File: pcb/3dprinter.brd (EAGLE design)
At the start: 100 x 80 mm, 111 parts, among them IC1 NRF51822, IC1_REG REGULATOR, IC2_REG LP2985-3V3, Q1_BED MOSFET, Q1_FAN1 MOSFETSOT23, Q1_FAN2 MOSFETSOT23, Q1_NOZ MOSFET, Y1 CRYSTAL

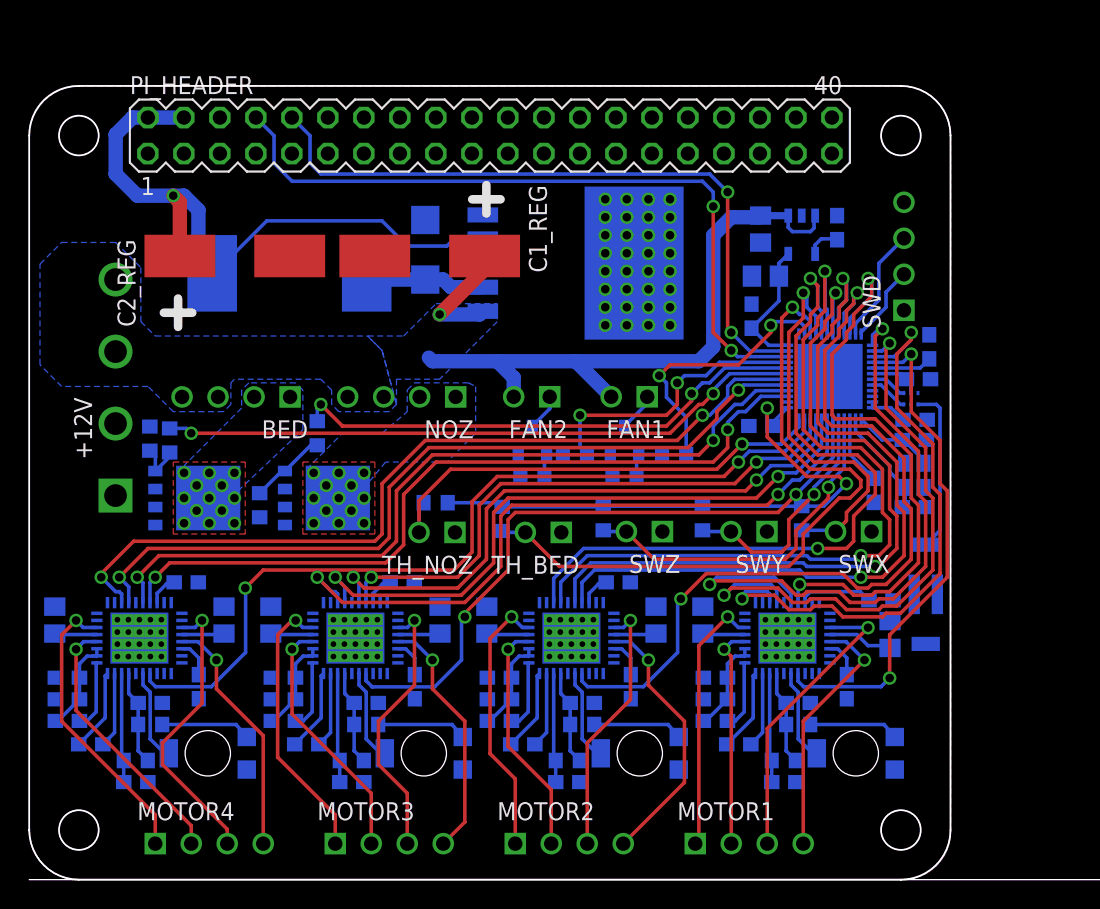
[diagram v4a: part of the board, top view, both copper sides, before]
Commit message: Component placement done, started final routing
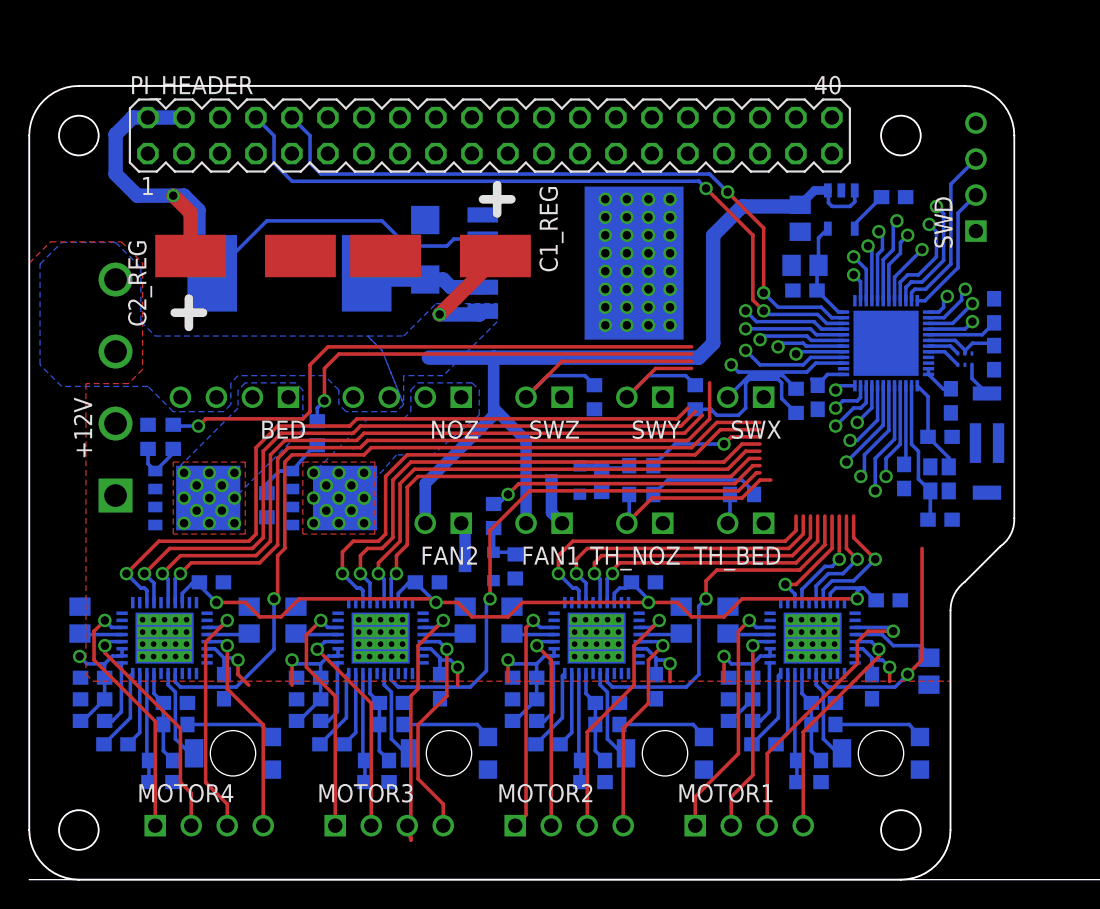
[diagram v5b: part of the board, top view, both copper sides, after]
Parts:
- moved R3_BED 17.0 mm to (50.3, 27.2), turned to 180 degrees
- moved TH_NOZ 14.7 mm to (42.2, 25.1)
- moved R3_NOZ 14.5 mm to (43.2, 27.2)
- moved TH_BED 14.3 mm to (49.3, 25.1)
- moved SWX 12.2 mm to (49.3, 34.0)
- moved SWY 12.0 mm to (42.2, 34.0)
- moved SWZ 11.8 mm to (35.1, 34.0)
- moved ANT 11.5 mm to (67.6, 30.8)
- moved FAN2 10.9 mm to (27.9, 25.1)
- moved FAN1 10.8 mm to (35.1, 25.1)
- moved Q1_FAN2 9.66 mm to (31.8, 22.1), turned to 180 degrees
- moved R1_SWZ 8.56 mm to (39.9, 34.0), turned to 270 degrees
- moved R1_SWY 8.55 mm to (47.0, 34.0), turned to 270 degrees
- moved R1_SWX 8.29 mm to (54.1, 33.8), turned to 270 degrees
- moved SWD 7.55 mm to (66.8, 49.6)
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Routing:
- net +12V: track 91.0 -> 134.9 mm, vias 1 -> 9
- net THBED: track 49.1 -> 5.56 mm
- net STEP_M1: track 44.3 -> 10.3 mm
- net +3V3: track 62.4 -> 95.1 mm, vias 2 -> 4
- net DIR_M2: track 54.3 -> 24.0 mm
- net CFG2_M1: track 41.6 -> 11.9 mm
- net CFG1_M1: track 40.9 -> 11.2 mm
- net CFG1_M2: track 54.5 -> 27.4 mm
- net STEP_M2: track 51.4 -> 25.6 mm
- net EN_M2: track 57.8 -> 32.9 mm
- net CFG2_M2: track 52.2 -> 27.7 mm
- net DIR_M1: track 41.1 -> 17.6 mm
- net THNOZ: track 34.0 -> 15.0 mm
- net SWX: track 27.9 -> 9.81 mm
- net EN_M1: track 36.0 -> 19.7 mm
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- added copper zone on layer 1, net +12V
- removed copper zone on layer 1, net GND
- removed copper zone on layer 16, net GND

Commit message: More routing
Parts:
- added SJ1, SJ2, SJ3, SJ4, SJ5, SJ6, SJ7, SJ8: (no value), 3dprinter:SJ_2
- moved R1_FAN2 11.6 mm to (43.2, 30.7), turned to 0 degrees
- moved Q1_FAN2 6.18 mm to (30.7, 28.2)
- moved R2_FAN2 6.18 mm to (33.3, 28.2)
- moved R2_M1 1.62 mm to (62.3, 13.6)
- moved C14 0.25 mm to (55.6, 33.8)
- moved C6_M4 0.25 mm to (13.1, 21.0)
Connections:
- new net P0.08: IC1.14
- new net P0.09: IC1.15
- new net P0.10: IC1.16
- new net P0.11: IC1.17
- new net P0.12: IC1.18
- new net P0.13: IC1.19
- new net P0.17: IC1.25
- new net P0.21: IC1.40
- net +3V3: now also SJ1.3, SJ2.3, SJ3.3, SJ4.3, SJ5.3, SJ6.3, SJ7.3, SJ8.3
- net BED: now also IC1.9; no longer IC1.7
- net CFG1_M1: now also SJ1.2; no longer IC1.26
- net CFG1_M2: now also SJ3.2; no longer IC1.18
- net CFG1_M3: now also SJ5.2; no longer IC1.44
- net CFG1_M4: now also SJ7.2; no longer IC1.5
- net CFG2_M1: now also SJ2.2; no longer IC1.27
- net CFG2_M2: now also SJ4.2; no longer IC1.17
- net CFG2_M3: now also SJ6.2; no longer IC1.43
- net CFG2_M4: now also SJ8.2; no longer IC1.6
- net DIR_M1: now also IC1.27; no longer IC1.22
- net DIR_M2: now also IC1.21; no longer IC1.20
- net DIR_M3: now also IC1.42; no longer IC1.46
- net DIR_M4: now also IC1.46; no longer IC1.3
- net EN_M2: now also IC1.22; no longer IC1.21
- net EN_M3: now also IC1.41; no longer IC1.42
- net EN_M4: now also IC1.45; no longer IC1.47
- net FAN1: now also IC1.43; no longer IC1.14
- net FAN2: now also IC1.48; no longer IC1.9
- net GND: now also SJ1.1, SJ2.1, SJ3.1, SJ4.1, SJ5.1, SJ6.1, SJ7.1, SJ8.1
- net STEP_M1: now also IC1.26; no longer IC1.25
- net STEP_M2: now also IC1.20; no longer IC1.19
- net STEP_M3: now also IC1.44; no longer IC1.45
- net STEP_M4: now also IC1.47; no longer IC1.4
- net SWX: now also IC1.3; no longer IC1.16
- net SWY: now also IC1.4; no longer IC1.41
- net SWZ: now also IC1.5; no longer IC1.40
- net THBED: now also IC1.6; no longer IC1.15
- net THNOZ: now also IC1.7; no longer IC1.48
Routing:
- net +3V3: track 95.1 -> 170.5 mm, vias 4 -> 13
- net CFG2_M4: track 55.6 -> 5.44 mm, vias 2 -> 1
- net CFG1_M4: track 52.9 -> 10.5 mm, vias 2 -> 1
- net CFG2_M3: track 46.2 -> 7.08 mm, vias 2 -> 1
- net CFG1_M3: track 42.4 -> 12.9 mm, vias 2 -> 1
- net STEP_M1: track 10.3 -> 33.8 mm
- net DIR_M2: track 24.0 -> 46.9 mm
- net STEP_M2: track 25.6 -> 46.9 mm
- net CFG2_M2: track 27.7 -> 7.37 mm, vias 2 -> 1
- net EN_M2: track 32.9 -> 52.1 mm
- net EN_M1: track 19.7 -> 38.5 mm
- net EN_M3: track 45.8 -> 64.2 mm
- net THBED: track 5.56 -> 23.8 mm
- net THNOZ: track 15.0 -> 32.5 mm
- net CFG1_M2: track 27.4 -> 12.7 mm, vias 2 -> 1
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- added copper zone on layer 1, net GND
- added copper zone on layer 16, net GND

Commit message: Final routing first pass
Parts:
- moved C1 0.80 mm to (67.3, 36.6)
- moved BAL 0.51 mm to (65.5, 36.7)
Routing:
- net GND: track 0.00 -> 68.0 mm, vias 32 -> 44
- net +3V3: track 170.5 -> 179.0 mm, vias 13 -> 15
- net OB1_M3: track 19.1 -> 17.2 mm
- net IC1_VDD_PA: track 5.62 -> 4.61 mm
- net ANT: track 2.76 -> 3.43 mm
- net IC1_ANT2: track 2.28 -> 1.77 mm
- net IC1_ANT1: track 2.44 -> 1.94 mm
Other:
- board size 100 x 80 mm -> 69.5 x 56 mm

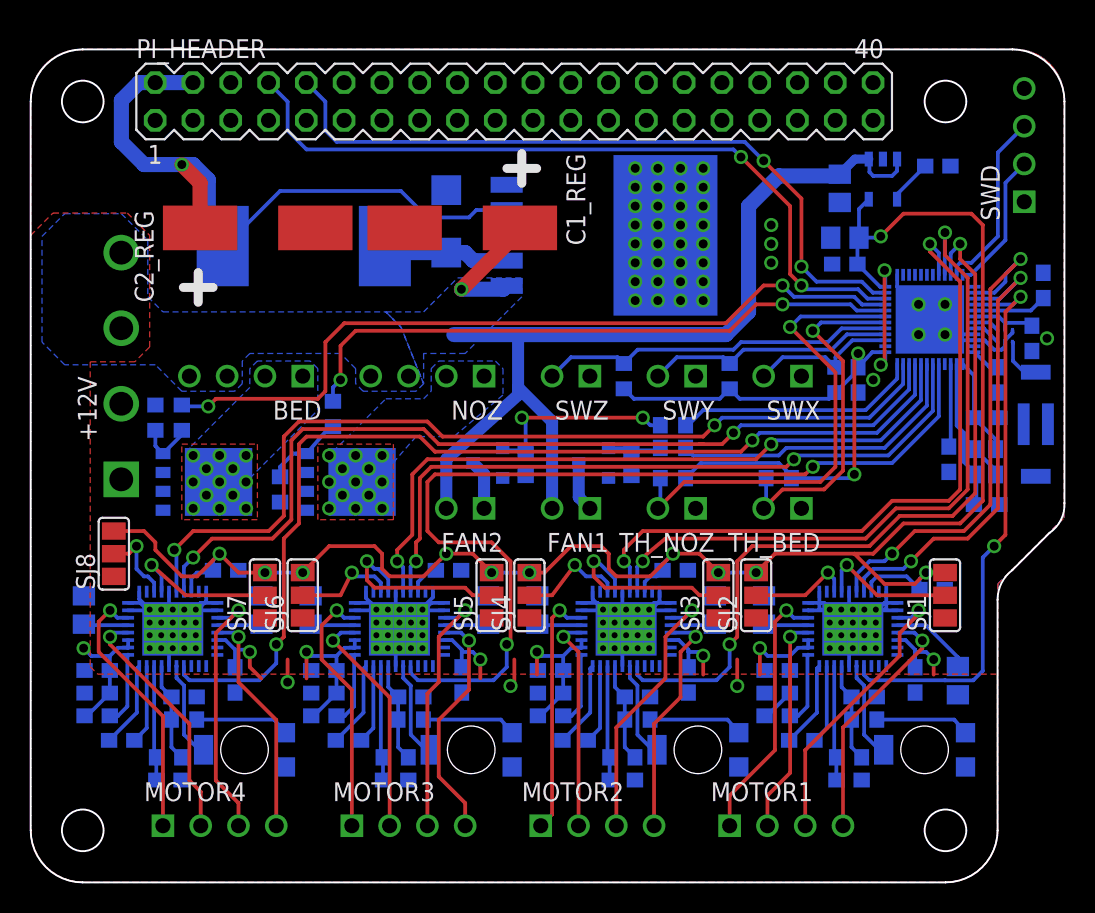
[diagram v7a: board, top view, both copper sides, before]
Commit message: Final routing, wire width, via drill, DRC approved
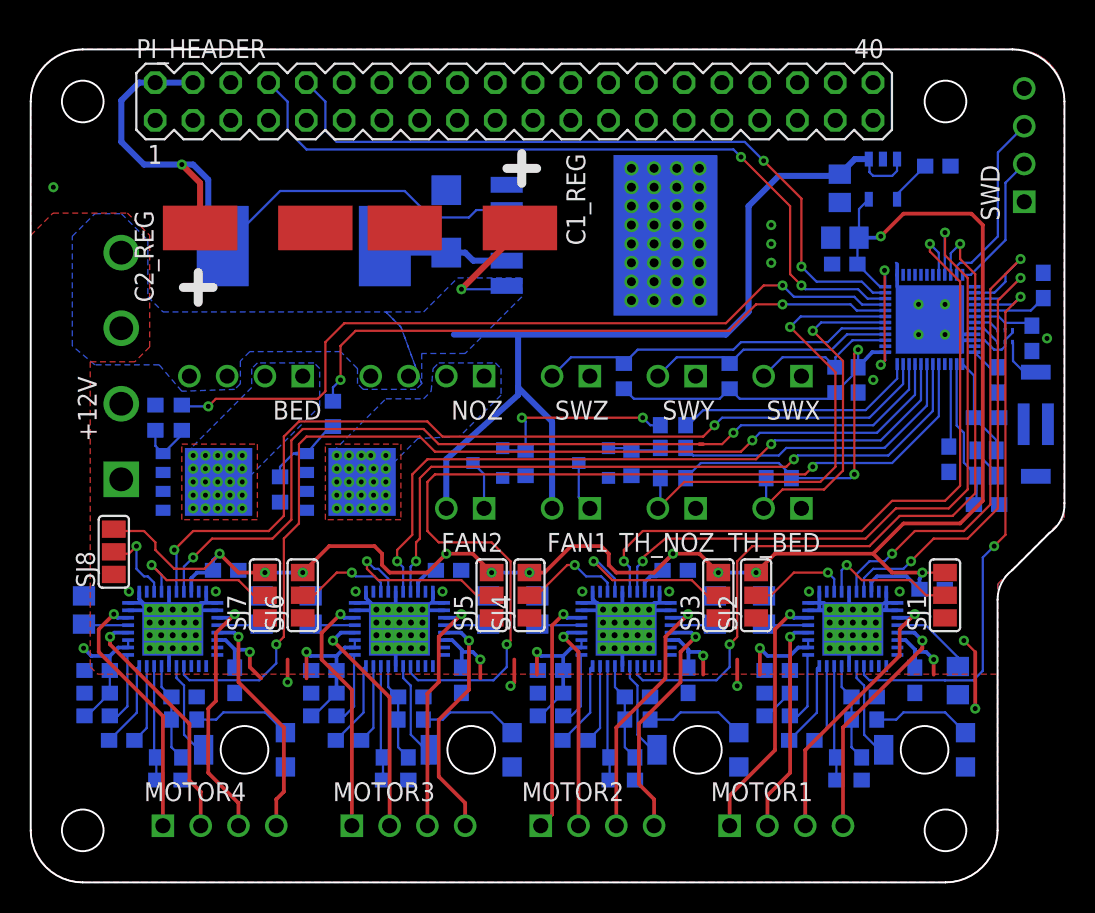
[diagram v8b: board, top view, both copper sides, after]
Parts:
- moved SJ8 0.13 mm to (5.59, 22.2)
- moved Y1 0.09 mm to (64.3, 28.2)
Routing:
- net GND: track 68.0 -> 73.7 mm, vias 44 -> 55
- net +3V3: track 179.0 -> 176.4 mm
- net OB2_M2: track 15.6 -> 16.5 mm
- net OB1_M2: track 18.2 -> 17.5 mm
- net OB1_M3: track 17.2 -> 16.4 mm
- net OB1_M1: track 19.3 -> 18.5 mm
- net CFG1_M2: track 12.7 -> 12.1 mm
- net OA1_M4: track 18.0 -> 17.5 mm
- net OA1_M3: track 17.2 -> 16.7 mm
- net OA1_M2: track 16.7 -> 16.2 mm
- net OA1_M1: track 17.7 -> 17.2 mm
